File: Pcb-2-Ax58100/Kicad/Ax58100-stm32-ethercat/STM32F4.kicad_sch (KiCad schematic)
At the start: 34 parts, among them J1 Conn_01x02_Pin, J2 STLINK, J3 Conn_01x06_Pin, J4 Conn_01x06_Pin, J5 Conn_01x06_Pin, J6 Serial usart1, J7 Stepper 1, J8 Stepper 2, U4 AMS1117-3.3, Y2 8 MHz

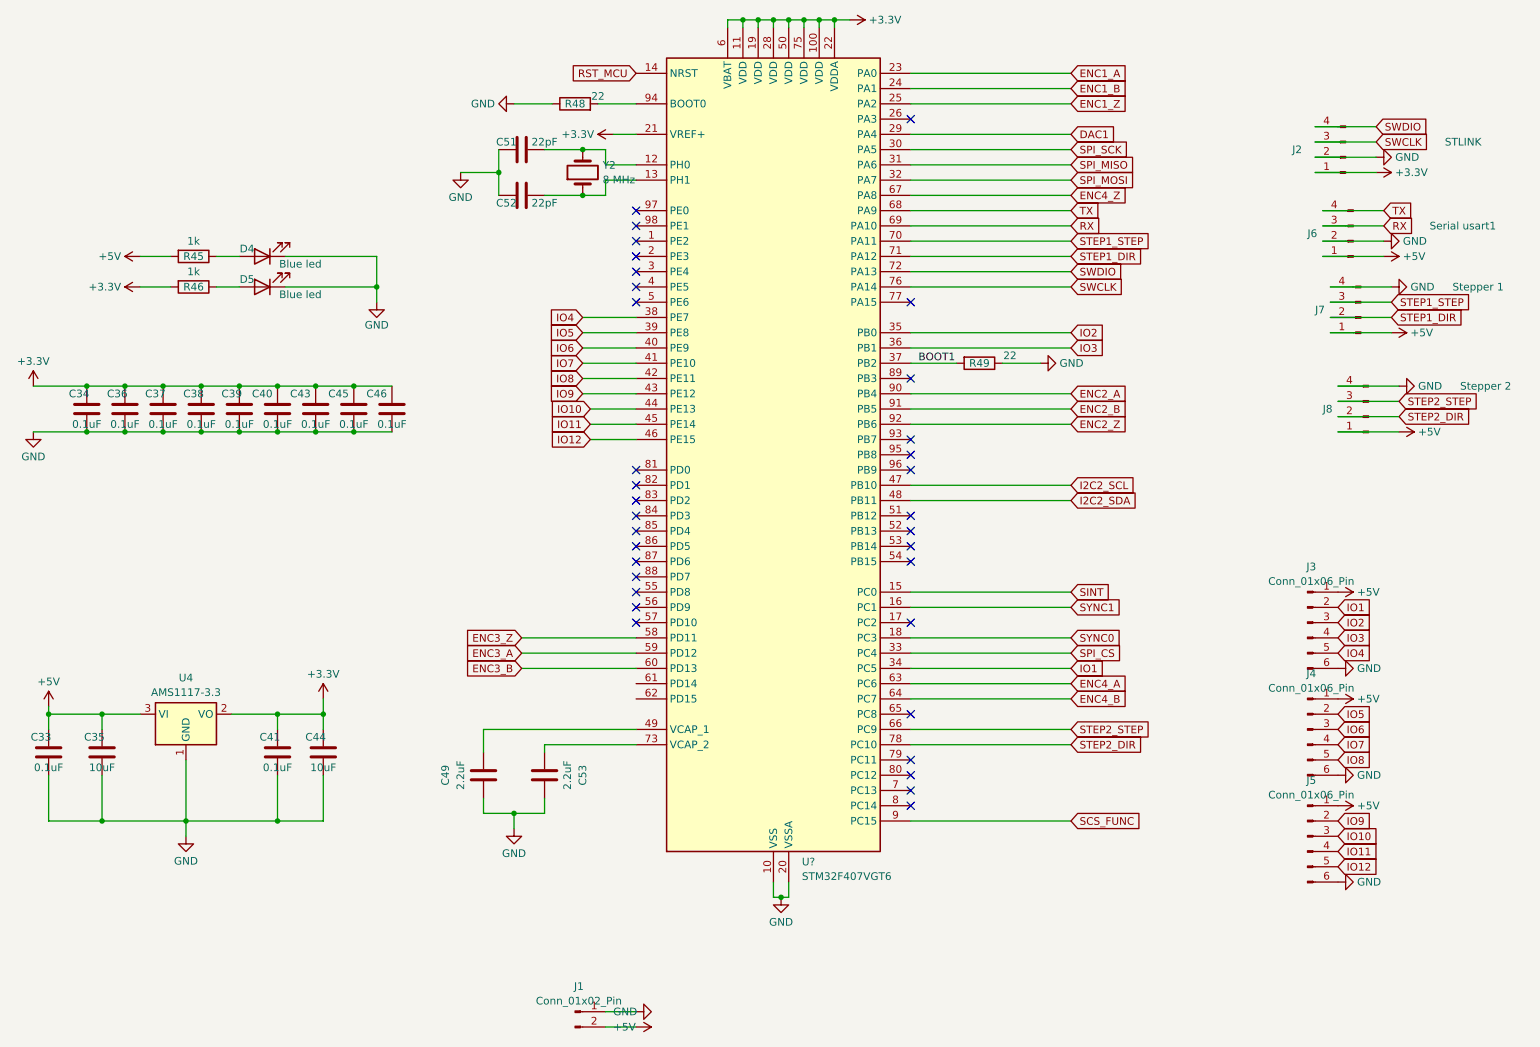
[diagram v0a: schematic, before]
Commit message: Geographic annotation on pcb 2
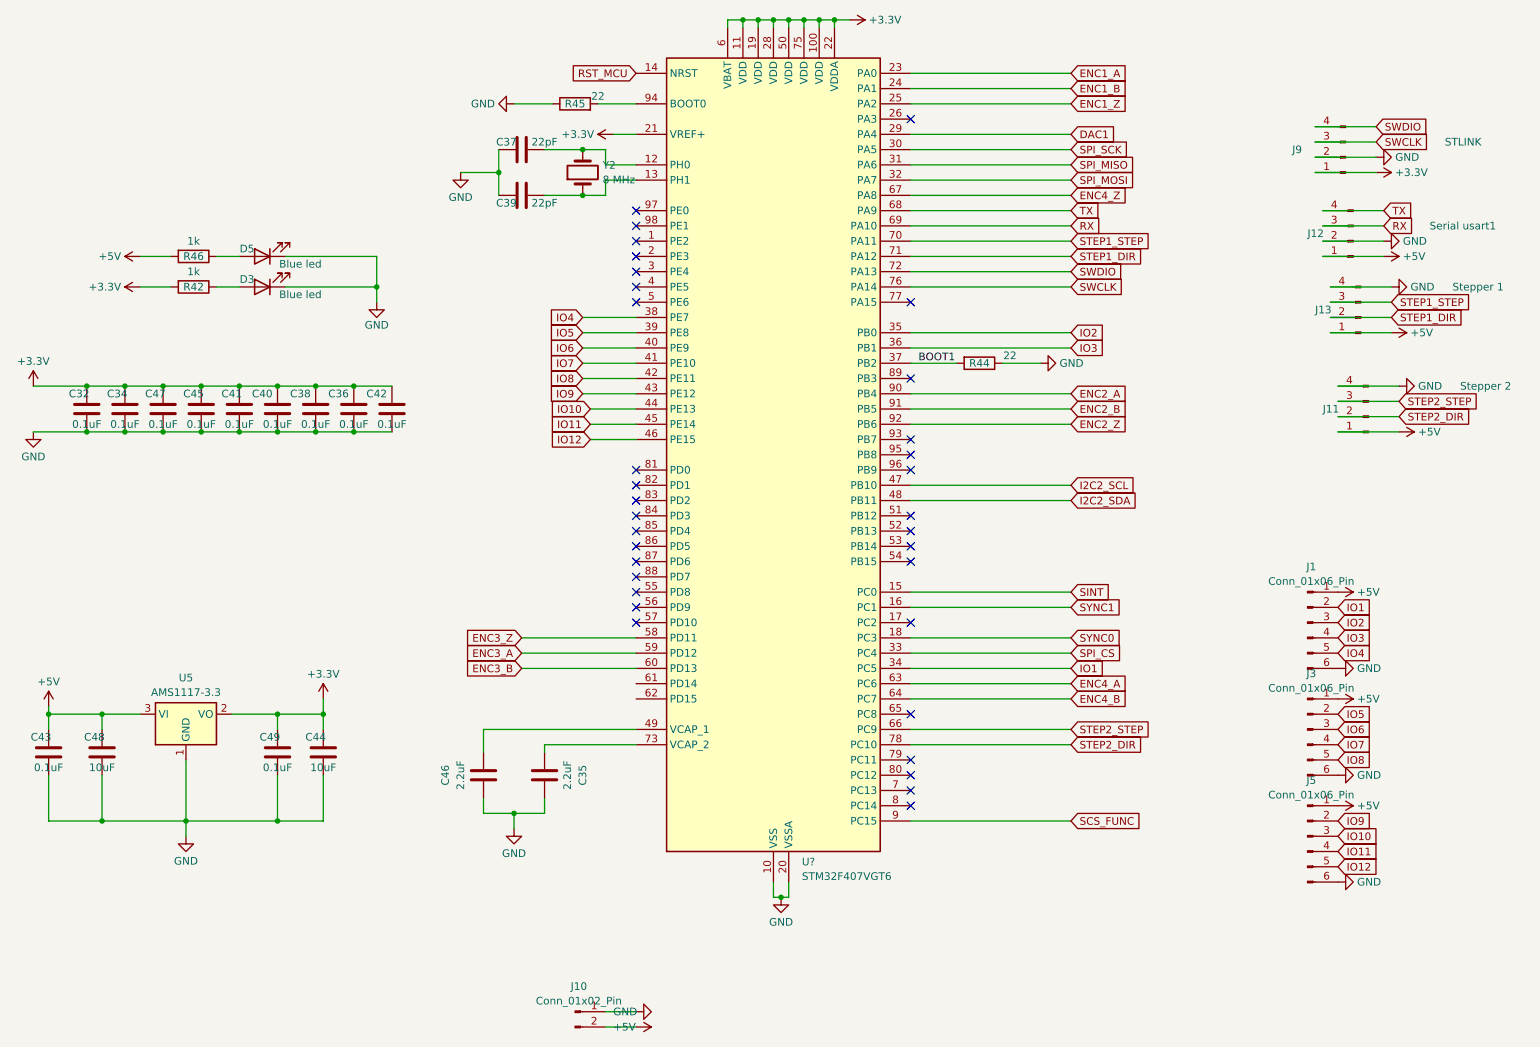
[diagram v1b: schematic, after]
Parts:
- renumbered C34 to C32, C36 to C34, C53 to C35, C45 to C36, C51 to C37, C43 to C38, C52 to C39, C39 to C41, C46 to C42, C33 to C43, C38 to C45, C49 to C46, C37 to C47, C35 to C48, C41 to C49, D5 to D3, D4 to D5, J3 to J1, J1 to J10, J8 to J11, J6 to J12, J7 to J13, J4 to J3, J2 to J9, R46 to R42, R49 to R44, R48 to R45, R45 to R46, U4 to U5
